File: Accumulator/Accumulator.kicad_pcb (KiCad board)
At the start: 2 copper layers, 220 x 160 mm, 23 parts, among them J1 16-way-pcb-edge-Educ-8-connec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, J2 16-way-pcb-edge-Educ-8-connec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, U1 74LS95, U10 74LS01, U2 74LS05, U3 74LS95, U4 74LS05, U5 74LS01, U6 74LS04, U7 7400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

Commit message: Schematic update 2024-04-14 plus fixes
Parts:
- C1, C3: footprint Capacitor_THT:C_Rect_L11.0mm_W2.8mm_P10.00mm_MKT -> Capacitor_THT:C_Rect_L10.3mm_W4.5mm_P7.50mm_MKS4
- C2, C4: footprint Capacitor_THT:C_Rect_L7.0mm_W2.5mm_P5.00mm -> Capacitor_THT:C_Rect_L10.3mm_W4.5mm_P7.50mm_MKS4
- R4: footprint Resistor_THT:R_Axial_DIN0207_L6.3mm_D2.5mm_P15.24mm_Horizontal -> Resistor_THT:R_Axial_DIN0207_L6.3mm_D2.5mm_P10.16mm_Horizontal
- moved R3 72.6 mm to (275.5, 178.6)
- moved U2 72.6 mm to (173.6, 108.7)
- moved C1 72.6 mm to (246.3, 141.1)
- moved C3 72.6 mm to (204.5, 182.4)
- moved H1 72.6 mm to (143.5, 61.0)
- moved H2 72.6 mm to (263.5, 61.0)
- moved J1 72.6 mm to (246.2, 217.9)
- moved J2 72.6 mm to (92.9, 217.9)
- moved R1 72.6 mm to (159.0, 98.5)
- moved R2 72.6 mm to (250.3, 141.1)
- moved R4 72.6 mm to (159.0, 143.8)
- moved REF** 72.6 mm to (109.4, 66.8)
- moved U1 72.6 mm to (143.6, 108.7)
- moved U10 72.6 mm to (289.6, 178.7)
- moved U3 72.6 mm to (143.6, 143.7)
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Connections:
- J1 pad 10: ~{IOT_SHIFT} -> ~{IOT_Shift}
- R4 pad 2: Net-(R4-Pad2) -> AC4
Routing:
- net +5V: track 774.4 -> 671.5 mm
- net ~{IOT_Shift}: track 0.00 -> 88.4 mm, vias 0 -> 2
- net ~{IOT_SHIFT}: track 85.3 -> 0.00 mm, vias 2 -> 0
- net ~{T13.RAR}: track 85.3 -> 76.0 mm
- net A-BUS: track 322.0 -> 319.9 mm
- net Net-(U10-Pad2): track 125.4 -> 124.5 mm
- net ~{CLA}: track 373.6 -> 372.7 mm
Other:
- outline, holes or cut-outs redrawn
- board text added: "Designed by Jamieson Rowe 1974 Electronics Australia PCB By Gwyllym Suter 2024"
- board text removed: "Designed by Jamieson Rowe 1974 Electronics Australia PCB By Gwyllym Suter 2021"

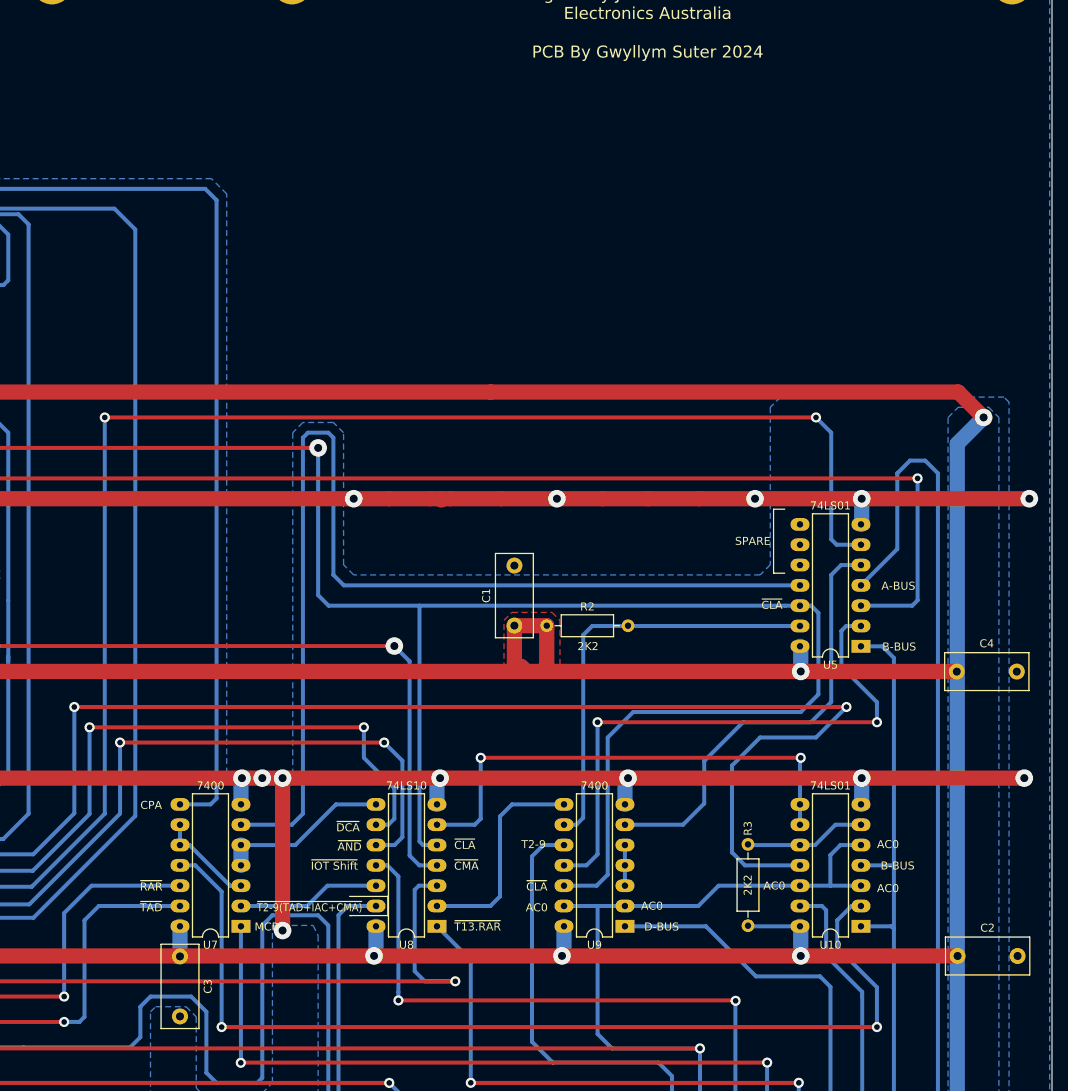
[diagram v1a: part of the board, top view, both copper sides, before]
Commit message: Changes 20-7-2025 E8/T. Connected 3 missing supply rail tracks to ICS Added flood fill top and bottom to reduce noise E8/F Corrected labelling on RHS board to reflect EXT_LA not GND Changed fast slow switch operation so fast is in the DOWN position. E8/C. Ran a new track to the 2 pin JST connector from EXT_LA from 10 pin connector on SR input. Added files for E8MX, 2k byte memory expansion board
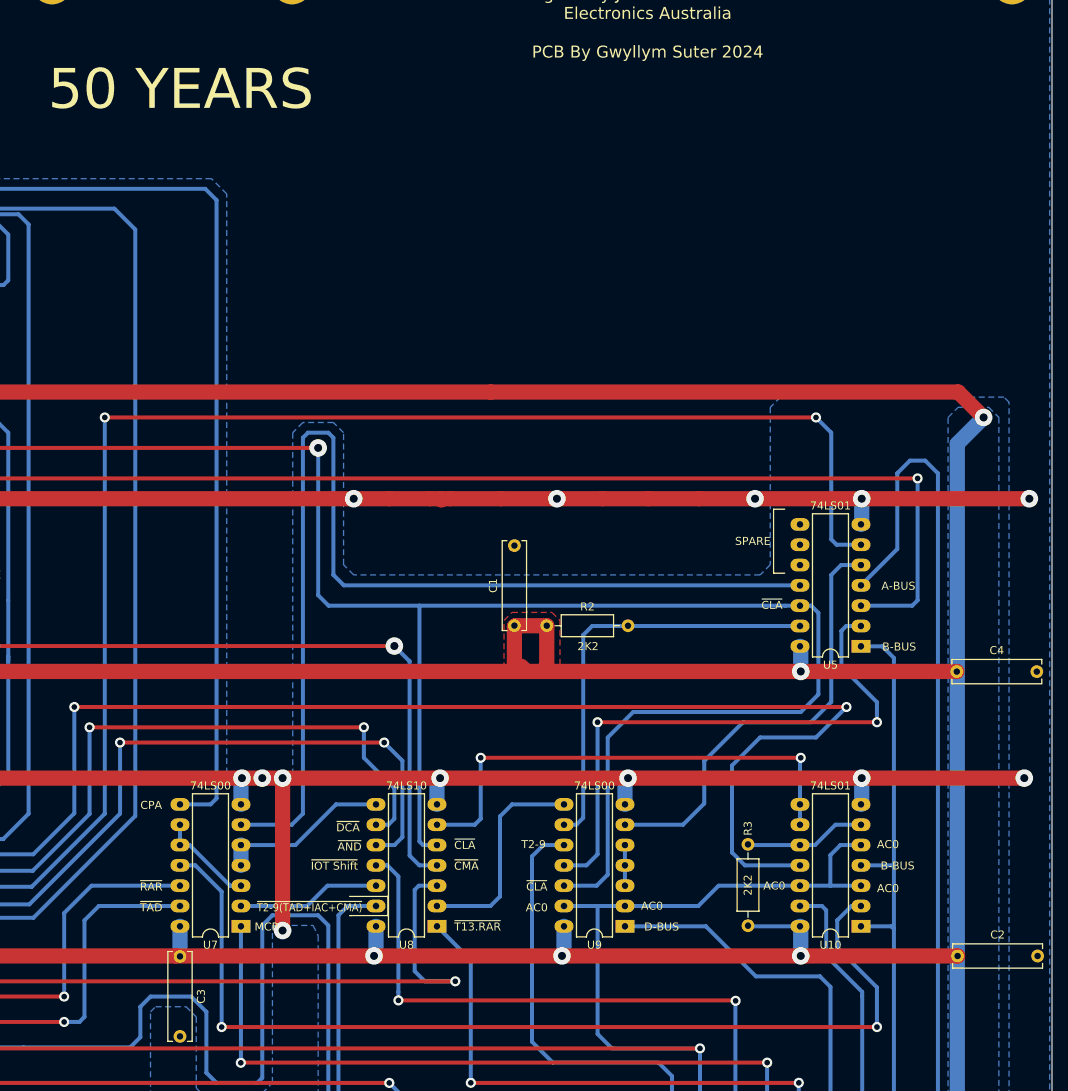
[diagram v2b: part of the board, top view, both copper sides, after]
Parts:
- C1, C2, C3, C4: footprint Capacitor_THT:C_Rect_L10.3mm_W4.5mm_P7.50mm_MKS4 -> Capacitor_THT:C_Rect_L11.0mm_W2.8mm_P10.00mm_MKT
- U7, U9: value 7400 -> 74LS00
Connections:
- R4 pad 2: AC4 -> Net-(R4-Pad2)
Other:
- board text added: "50 YEARS"
